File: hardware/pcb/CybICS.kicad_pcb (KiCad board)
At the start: 2 copper layers, 160 x 100 mm, 79 parts, among them J1 Raspberry_Pi_2_3, J2 Conn_01x03_Pin, J3 Conn_01x05_Pin, J4 USB_C_Receptacle_USB2.0, SW1 SW_Push, SW2 SW_Push, SW3 SW_Push, U1 STM32G070RBTx

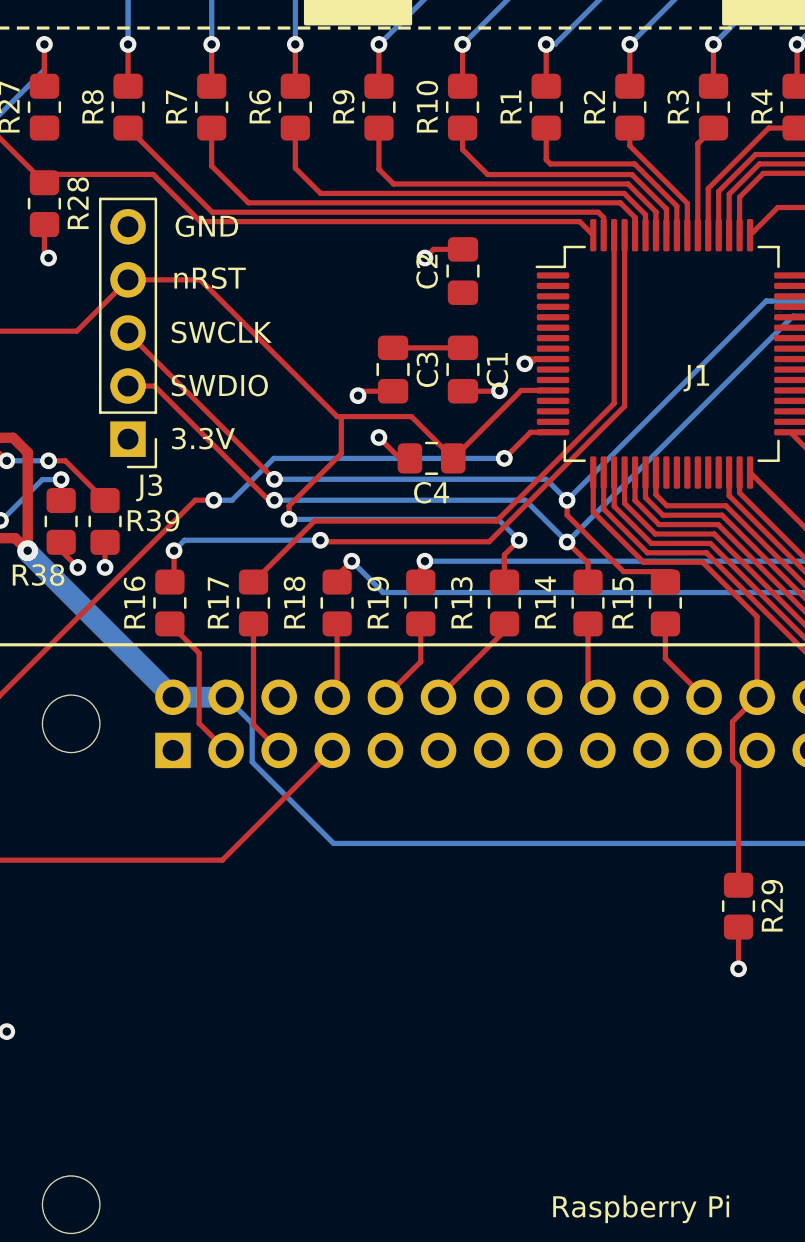
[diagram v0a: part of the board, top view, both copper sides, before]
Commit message: feat(hardware): add a 5-bit hardware version strap to the STM32 and the Pi
A new board revision needs to be identifiable from software, so both
controllers get a version code they can read back.

One 10k resistor per bit to GND, read against the controller's internal
pull-up: fitted = 0, omitted = 1. That keeps it to a single part per bit,
and future revisions are then a pure assembly change -- no schematic or
layout edit to bump the version. The value is C17414, which the board
already carries nine times, so the BOM gains no line and no feeder fee;
the ten straps group into the existing 10kR row (R28-R36,R40-R44,R46-R50).

Pins were picked for contiguity on the board rather than in the
schematic, because routing was the constraint:

  HWV_STM0..4  U1 pins 1-5    PC11, PC12, PC13, PC14, PC15
  HWV_RPI0..4  J1 11,13,15    GPIO17, GPIO27, GPIO22
               J1 16,19       GPIO23, GPIO10

PC14/PC15 are the LSE oscillator pins and PF0/PF1 the HSE pins; the board
fits no crystal, so the former are free to use and the latter were still
left alone. SPI0 clock and ID_SD/GPIO0 (reserved for the HAT EEPROM) were
kept clear; GPIO10 is MOSI0 and is the one compromise, taken because the
corridor south of J1 pins 23/29/31 is blocked by the LCD's fan-out.

All ten straps route north to their pin and drop south through a via into
the B.Cu GND plane, so the ground side needed no routing at all.

Nothing else was rewired, and that is checked rather than asserted: of
the 108 nets the design had before, 107 have byte-identical node sets
afterwards. The single exception is GND, which gained ten nodes and lost
none. The ten new nets carry exactly two nodes each.

Designators sit north of their parts at 3.6 mm, rotated vertical. The
library default put them 1.65 mm east, where they collided with the next
resistor in the 2 mm pitch; 2.5 mm north still placed every label over
its own pad, where the silkscreen would have been clipped in production.
Silkscreen warnings across the board dro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
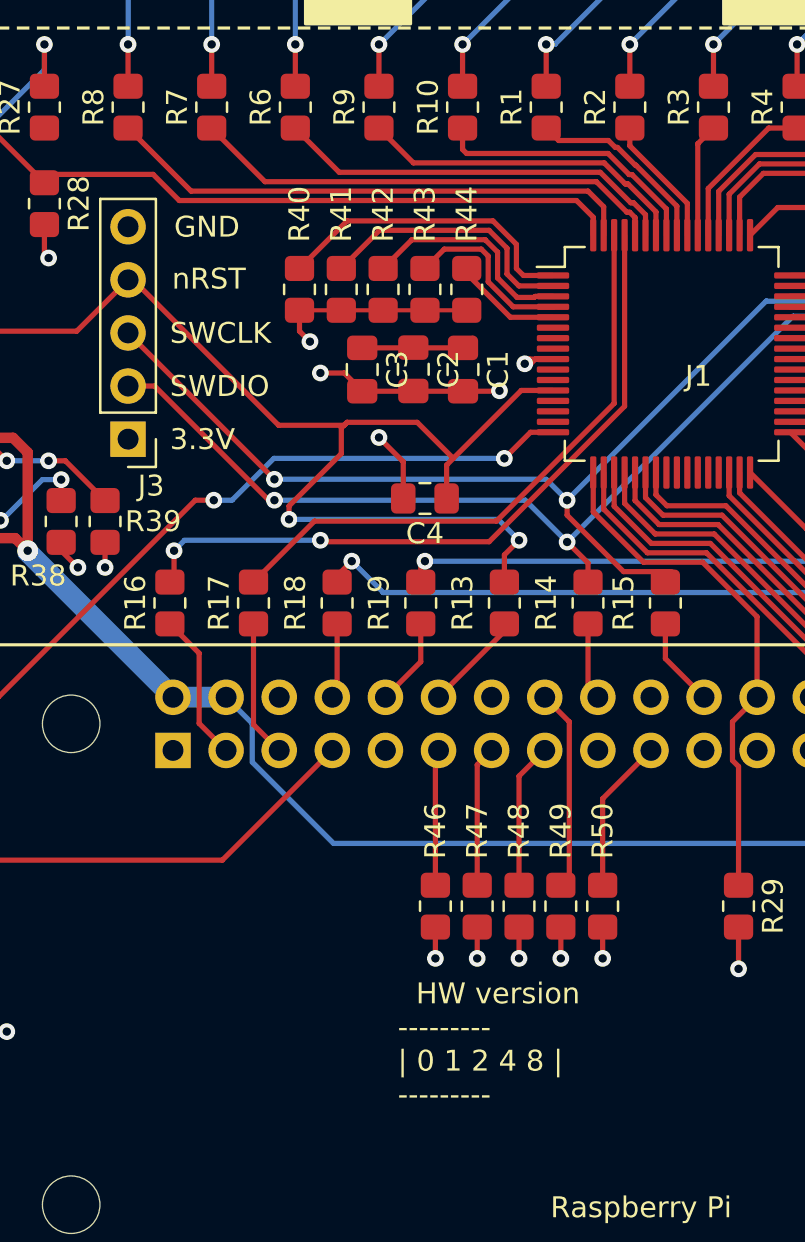
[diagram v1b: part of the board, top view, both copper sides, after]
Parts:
- added R40: 10kR, Resistor_SMD:R_0805_2012Metric_Pad1.20x1.40mm_HandSolder, F.Cu at (77.0, 103.5)
- added R41: 10kR, Resistor_SMD:R_0805_2012Metric_Pad1.20x1.40mm_HandSolder, F.Cu at (79.0, 103.5)
- added R42: 10kR, Resistor_SMD:R_0805_2012Metric_Pad1.20x1.40mm_HandSolder, F.Cu at (81.0, 103.5)
- added R43: 10kR, Resistor_SMD:R_0805_2012Metric_Pad1.20x1.40mm_HandSolder, F.Cu at (83.0, 103.5)
- added R44: 10kR, Resistor_SMD:R_0805_2012Metric_Pad1.20x1.40mm_HandSolder, F.Cu at (85.0, 103.5)
- added R46: 10kR, Resistor_SMD:R_0805_2012Metric_Pad1.20x1.40mm_HandSolder, F.Cu at (83.5, 133.0)
- added R47: 10kR, Resistor_SMD:R_0805_2012Metric_Pad1.20x1.40mm_HandSolder, F.Cu at (85.5, 133.0)
- added R48: 10kR, Resistor_SMD:R_0805_2012Metric_Pad1.20x1.40mm_HandSolder, F.Cu at (87.5, 133.0)
- added R49: 10kR, Resistor_SMD:R_0805_2012Metric_Pad1.20x1.40mm_HandSolder, F.Cu at (89.5, 133.0)
- added R50: 10kR, Resistor_SMD:R_0805_2012Metric_Pad1.20x1.40mm_HandSolder, F.Cu at (91.5, 133.0)
- moved C2 5.27 mm to (82.4, 107.3), turned to -90 degrees
- moved C4 1.94 mm to (83.0, 113.5)
- moved C3 1.47 mm to (80.0, 107.3)
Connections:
- J1 pad 11: unconnected-(J1-GPIO17-Pad11) -> /HWV_RPI0
- J1 pad 13: unconnected-(J1-GPIO27-Pad13) -> /HWV_RPI1
- J1 pad 15: unconnected-(J1-GPIO22-Pad15) -> /HWV_RPI2
- J1 pad 16: unconnected-(J1-GPIO23-Pad16) -> /HWV_RPI3
- J1 pad 19: unconnected-(J1-MOSI0/GPIO10-Pad19) -> /HWV_RPI4
- U1 pad 1: unconnected-(U1-PC11-Pad1) -> /HWV_STM0
- U1 pad 2: unconnected-(U1-PC12-Pad2) -> /HWV_STM1
- U1 pad 3: unconnected-(U1-PC13-Pad3) -> /HWV_STM2
- U1 pad 4: unconnected-(U1-PC14-Pad4) -> /HWV_STM3
- U1 pad 5: unconnected-(U1-PC15-Pad5) -> /HWV_STM4
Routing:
- net /HWV_STM0: track 0.00 -> 14.8 mm
- net GND: track 40.3 -> 54.5 mm, vias 20 -> 25
- net /HWV_STM1: track 0.00 -> 12.7 mm
- net /HWV_STM2: track 0.00 -> 10.6 mm
- net /HWV_RPI3: track 0.00 -> 9.64 mm
- net /HWV_STM3: track 0.00 -> 8.37 mm
- net /HWV_RPI4: track 0.00 -> 7.41 mm
- net /HWV_RPI2: track 0.00 -> 6.96 mm
- net /HWV_RPI1: track 0.00 -> 6.74 mm
- net /HWV_RPI0: track 0.00 -> 6.51 mm
- net /HWV_STM4: track 0.00 -> 5.24 mm
- net /STMnrst: track 60.6 -> 62.2 mm
- net /PB4: track 17.2 -> 16.0 mm
- net /PB5: track 20.6 -> 19.5 mm
- net +3V3: track 4.44 -> 5.54 mm
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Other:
- board text added: "HW version --------- | 0 1 2 4 8 | ---------"

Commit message: feat(hardware)!: encode this revision as hardware version 1.1
The straps from the previous commit were all fitted, so both controllers
reported code 0. This assigns the revision properly: bit 0 is omitted on
each side (R40 for the STM32, R46 for the Pi), giving `00001` = 1 = v1.1.
One resistor per side, because the two controllers read independent 5-bit
sets and must agree on the version.

The copper lettering moves with it: "CybICS v1.0" -> "CybICS v1.1" on
F.Cu and its F.Mask opening, so the board states its own revision.

Worth recording why 31 is reserved rather than used: a v1.0 board has no
strap footprints at all, so those pins float and the internal pull-ups
make it read `11111`. Every pre-v1.1 board therefore identifies itself
without any change to it, which is the useful half. The other half is
that a v1.1 board assembled with no straps reads the same, so 31 means
"pre-v1.1, or straps missing" and cannot be given to a real revision.

R40 and R46 carry `(dnp yes)` in the schematic and `dnp` in the footprint
attributes. Verified both ways with kicad-cli 10.0.6: `sch export bom
--exclude-dnp` yields R28-R36,R41-R44,R47-R50 with R40/R46 gone, and
without the flag they appear marked DNP; `pcb export pos --exclude-dnp`
gives 74 rows against 76 without it, with R40 and R46 absent. Whether
JLCPCB actually receives them depends on the Fabrication Toolkit
honouring DNP, so the ordering guide now has an explicit check for it --
if they get placed, the board reports the wrong revision.

Documented in hardware/README.md with the bit-to-pin table and the code
table, and CLAUDE.md gains the F8 trap found while verifying this: Update
PCB from Schematic resets footprint attributes from the library and
silently drops exclude_from_pos_files from FID1-FID3 and H1-H3, which
puts the #238 fiducials straight back into the position file.

Verified: ERC, DRC and schematic parity all 0 violations and 0
unconnected items after the copper lettering change; all four
kibotVerify.yml ge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
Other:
- board text added: "CybICS v1.1"
- board text removed: "CybICS v1.0"
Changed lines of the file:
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@@
 			)
 		)
-		(attr smd)
+		(attr smd dnp)
 		(duplicate_pad_numbers_are_jumpers no)
 		(fp_line
@@
 			)
 		)
-		(attr smd)
+		(attr smd dnp)
 		(duplicate_pad_numbers_are_jumpers no)
 		(fp_line
@@
 		(layer "Edge.Cuts")
 	)
-	(gr_text "CybICS v1.0"
+	(gr_text "CybICS v1.1"
 		(at 76.8 59.8 0)
 		(layer "F.Cu")
@@
 		)
 	)
-	(gr_text "CybICS v1.0\n"
+	(gr_text "CybICS v1.1\n"
 		(at 76.8 59.8 0)
 		(layer "F.Mask")

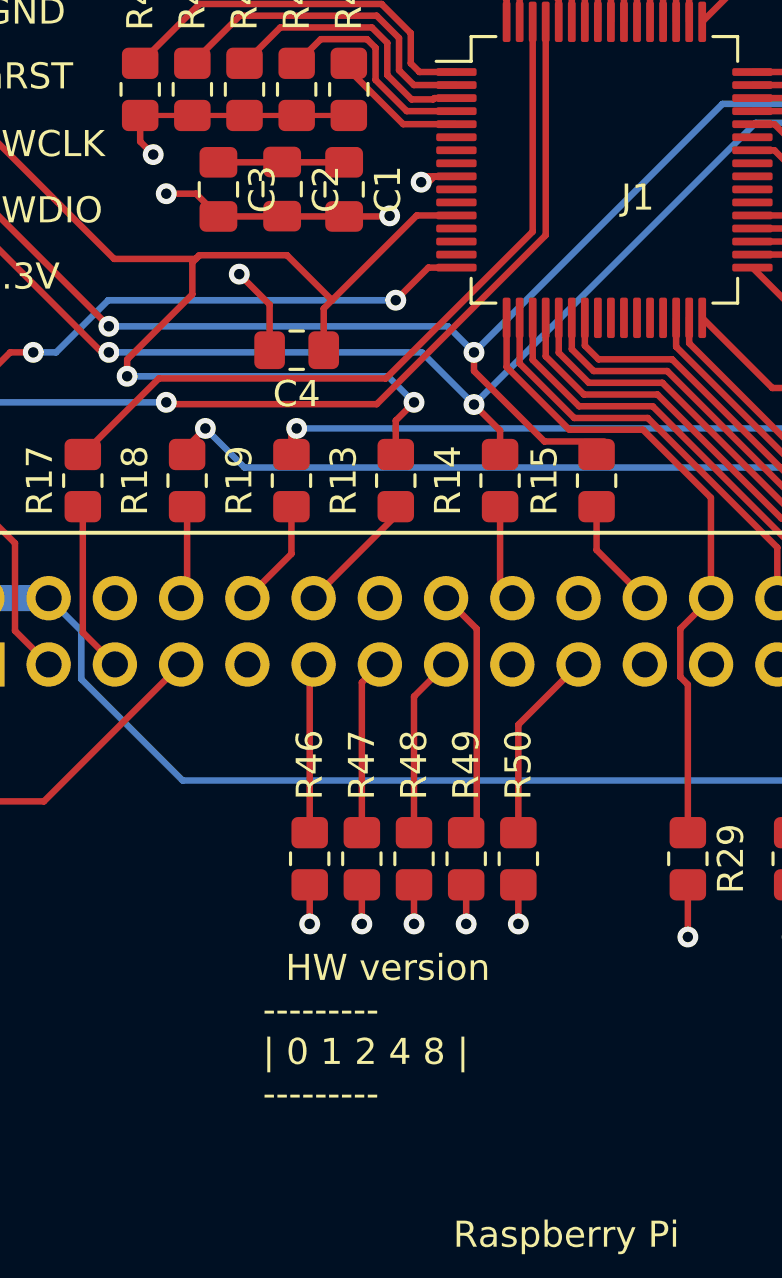
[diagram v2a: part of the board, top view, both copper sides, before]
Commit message: fix(hardware): move the capacitor designators south of their parts
C1, C2 and C3 sit at -90 degrees about 2.4 mm apart, and the library
default put each reference field 1.68 mm east -- straight onto the next
capacitor's pads. DRC reported it four times as silk_over_copper: C2's
field over C1's +3V3 and GND pads, C3's field over C2's. Silkscreen over
an exposed pad is clipped in production, so those labels would have come
out incomplete.

Moved to 2.4 mm south, horizontal, which is where C4 already had its
designator -- so the four now read as one consistent group rather than
three-plus-one. 2.8 mm was equally clean in DRC; 2.4 mm keeps the label
closer to its part.

With this the board is free of silkscreen findings at every severity:
`kicad-cli pcb drc --refill-zones --severity-all` reports 0 violations
and 0 unconnected items, down from 28 before the designator work started.
Schematic parity and ERC are also 0, all four kibotVerify.yml generating
jobs exit 0, and the area was rendered and inspected. pytest tests/
against the live stack: 76 passed, 1 skipped.

Co-Authored-By: Claude Opus 5 (1M context) <noreply@anthropic.com>
Claude-Session: https://claude.ai/code/session_011zbigHZaGiZii3etPu8DwT
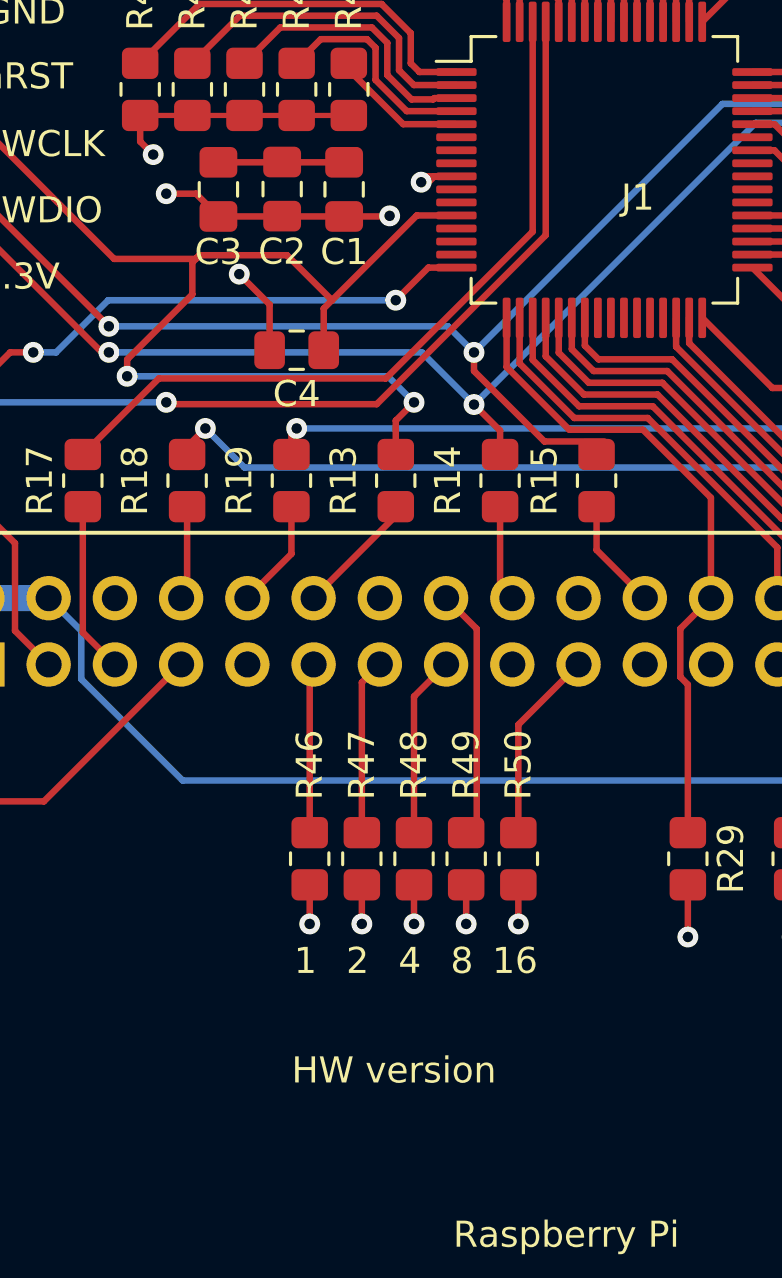
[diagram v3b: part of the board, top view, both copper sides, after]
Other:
- board text added: "1"
- board text added: "16"
- board text added: "2"
- board text added: "4"
- board text added: "8"
- board text added: "HW version"
- board text removed: "HW version --------- | 0 1 2 4 8 | ---------"
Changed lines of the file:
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@@
 		(tags "capacitor handsolder")
 		(property "Reference" "C2"
-			(at 0 -1.68 90)
+			(at 2.4 0 0)
 			(layer "F.SilkS")
 			(effects
@@
 		(tags "capacitor handsolder")
 		(property "Reference" "C3"
-			(at 0 -1.68 90)
+			(at 2.4 0 0)
 			(layer "F.SilkS")
 			(effects
@@
 		(tags "capacitor handsolder")
 		(property "Reference" "C1"
-			(at 0 -1.68 90)
+			(at 2.4 0 0)
 			(layer "F.SilkS")
 			(effects
@@
 		)
 	)
-	(gr_text "  HW version\n---------\n| 0 1 2 4 8 |\n---------"
-		(at 81.7 142.6 0)
+	(gr_text "\n   HW version"
+		(at 81.5 141.7 0)
+		(layer "F.SilkS")
+		(effects
+			(font
+				(size 1 1)
+				(thickness 0.25)
+			)
+			(justify left bottom)
+		)
+	)
+	(gr_text "1"
+		(at 82.9 137.5 0)
+		(layer "F.SilkS")
+		(effects
+			(font
+				(size 1 1)
+				(thickness 0.25)
+			)
+			(justify left bottom)
+		)
+	)
+	(gr_text "2"
+		(at 84.9 137.5 0)
+		(layer "F.SilkS")
+		(effects
+			(font
+				(size 1 1)
+				(thickness 0.25)
+			)
+			(justify left bottom)
+		)
+	)
+	(gr_text "4"
+		(at 86.9 137.5 0)
+		(layer "F.SilkS")
+		(effects
+			(font
+				(size 1 1)
+				(thickness 0.25)
+			)
+			(justify left bottom)
+		)
+	)
+	(gr_text "8"
+		(at 88.9 137.5 0)
+		(layer "F.SilkS")
+		(effects
+			(font
+				(size 1 1)
+				(thickness 0.25)
+			)
+			(justify left bottom)
+		)
+	)
+	(gr_text "16"
+		(at 90.5 137.5 0)
 		(layer "F.SilkS")
 		(effects

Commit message: fix(hardware): size the strap resistors and give the switch series limits
Two changes that both come down to reading a pin low reliably against the
STM32G0's weak pull-up, which the datasheet puts at 25k minimum, 40k
typical, 60k maximum.

The version straps were 10k. That is a divider against the internal
pull-up, and at the 25k end it sits at 0.94 V -- roughly 50 mV under a
V_IL of 0.3*VDD. Designed to the typical value it looks fine at 0.66 V,
but worst-case silicon could read a fitted strap as high. At 1k the same
worst case is 0.127 V, a margin of 0.86 V instead of 0.05 V. Current
through a fitted strap is 53-127 uA, which is nothing. C17513 is already
a basic part in this BOM, so the ten straps just move from the 10kR row
to the 1kR row and cost no new line and no feeder fee. R40 and R46 keep
their DNP flags, verified in both the schematic and the board.

The navigation switch gets a 1k in series with each of its five contacts
(R51-R55). This is not about levels -- a switch is a short or an open,
so the internal pull-up alone reads it correctly. It restores something
the old button had and this redesign had quietly dropped: R37 used to sit
in series, limiting the current if a pin were ever configured as an
output driving high while the button is pressed. Without it that is a
direct short to GND; with 1k it is 3.3 mA. 1k also keeps the closed-
contact level at 0.127 V worst case.

The common's GND leg was rerouted to x=248.92 so it clears the two
west-side resistors.

Verified with kicad-cli 10.0.6: ERC reports 0 violations and the netlist
shows each contact running SW3 -> 1k -> MCU pin, with SW3.2 on GND and
pins 7/8 unconnected. The switch area was rendered and checked.

Still to do on the board: Update PCB from Schematic, then place and route
R51-R55 -- they exist in the schematic only. The reference and value text
of the three east-side resistors still overlaps at the 5.08 mm pitch and
wants a nudge in eeschema.

Co-Authored-By: Claude Opus 5 (1M context) <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
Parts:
- R40, R41, R42, R43, R44, R46, R47, R48, R49, R50: value 10kR -> 1kR
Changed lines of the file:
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@@
 			)
 		)
-		(property "Value" "10kR"
+		(property "Value" "1kR"
 			(at 0 1.65 90)
 			(layer "F.Fab")
@@
 			)
 		)
-		(property "JLCPCB Part #" "C17414"
+		(property "JLCPCB Part #" "C17513"
 			(at 0 0 270)
 			(unlocked yes)
@@
 			)
 		)
-		(property "Value" "10kR"
+		(property "Value" "1kR"
 			(at 0 1.65 90)
 			(layer "F.Fab")
@@
 			)
 		)
-		(property "JLCPCB Part #" "C17414"
+		(property "JLCPCB Part #" "C17513"
 			(at 0 0 270)
 			(unlocked yes)
@@
 			)
 		)
-		(property "Value" "10kR"
+		(property "Value" "1kR"
 			(at 0 1.65 90)
 			(layer "F.Fab")
@@
 			)
 		)
-		(property "JLCPCB Part #" "C17414"
+		(property "JLCPCB Part #" "C17513"
 			(at 0 0 270)
 			(unlocked yes)
@@
 			)
 		)
-		(property "Value" "10kR"
+		(property "Value" "1kR"
 			(at 0 1.65 90)
 			(layer "F.Fab")
@@
 			)
 		)
-		(property "JLCPCB Part #" "C17414"
+		(property "JLCPCB Part #" "C17513"
 			(at 0 0 270)
 			(unlocked yes)
@@
 			)
 		)
-		(property "Value" "10kR"
+		(property "Value" "1kR"
 			(at 0 1.65 90)
 			(layer "F.Fab")
@@
 			)
 		)
-		(property "JLCPCB Part #" "C17414"
+		(property "JLCPCB Part #" "C17513"
 			(at 0 0 270)
 			(unlocked yes)
@@
 			)
 		)
-		(property "Value" "10kR"
+		(property "Value" "1kR"
 			(at 0 1.65 90)
 			(layer "F.Fab")
@@
 			)
 		)
-		(property "JLCPCB Part #" "C17414"
+		(property "JLCPCB Part #" "C17513"
 			(at 0 0 270)
 			(unlocked yes)
@@
 			)
 		)
-		(property "Value" "10kR"
+		(property "Value" "1kR"
 			(at 0 1.65 90)
 			(layer "F.Fab")
@@
 			)
 		)
-		(property "JLCPCB Part #" "C17414"
+		(property "JLCPCB Part #" "C17513"
 			(at 0 0 270)
 			(unlocked yes)
@@
 			)
 		)
-		(property "Value" "10kR"
+		(property "Value" "1kR"
 			(at 0 1.65 90)
 			(layer "F.Fab")
@@
 			)
 		)
-		(property "JLCPCB Part #" "C17414"
+		(property "JLCPCB Part #" "C17513"
 			(at 0 0 270)
 			(unlocked yes)
@@
 			)
 		)
-		(property "Value" "10kR"
+		(property "Value" "1kR"
 			(at 0 1.65 90)
 			(layer "F.Fab")
@@
 			)
 		)
-		(property "JLCPCB Part #" "C17414"
+		(property "JLCPCB Part #" "C17513"
 			(at 0 0 270)
 			(unlocked yes)
@@
 			)
 		)
-		(property "Value" "10kR"
+		(property "Value" "1kR"
 			(at 0 1.65 90)
 			(layer "F.Fab")
@@
 			)
 		)
-		(property "JLCPCB Part #" "C17414"
+		(property "JLCPCB Part #" "C17513"
 			(at 0 0 270)
 			(unlocked yes)
